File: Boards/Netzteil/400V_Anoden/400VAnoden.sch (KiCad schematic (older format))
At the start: 42 parts, among them P1 Drossel, P2 450V_AC, P3 CONN_4, P4 -120V_AC, P5 CONN_4, Q1 2SC2979

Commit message: Layouting...
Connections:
- wire segments 63 -> 61
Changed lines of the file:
@@
 EESchema Schematic File Version 2
+LIBS:400VAnoden-rescue
 LIBS:power
 LIBS:device
@@
 	8500 2700 8500 2600
 $Comp
-L GND #PWR10
+L GND-RESCUE-400VAnoden #PWR10
 U 1 1 55C60758
 P 8500 3250
@@
 $EndComp
 $Comp
-L GND #PWR8
+L GND-RESCUE-400VAnoden #PWR8
 U 1 1 55C607C2
 P 8100 2500
@@
 $EndComp
 $Comp
-L GND #PWR3
+L GND-RESCUE-400VAnoden #PWR3
 U 1 1 55C6080F
 P 1550 2250
@@
 $EndComp
 $Comp
-L GND #PWR4
+L GND-RESCUE-400VAnoden #PWR4
 U 1 1 55C60A98
 P 4350 2500
@@
 $EndComp
 $Comp
-L GND #PWR5
+L GND-RESCUE-400VAnoden #PWR5
 U 1 1 55C60AE5
 P 4950 2500
@@
 $EndComp
 $Comp
-L GND #PWR6
+L GND-RESCUE-400VAnoden #PWR6
 U 1 1 55C60B32
 P 6900 2500
@@
 $EndComp
 $Comp
-L GND #PWR7
+L GND-RESCUE-400VAnoden #PWR7
 U 1 1 55C60B7F
 P 7500 2500
@@
 $EndComp
 $Comp
-L GND #PWR1
+L GND-RESCUE-400VAnoden #PWR1
 U 1 1 55C60BCC
 P 5450 2000
@@
 $EndComp
 $Comp
-L GND #PWR2
+L GND-RESCUE-400VAnoden #PWR2
 U 1 1 55C60C19
 P 6250 2000
@@
 $EndComp
 Wire Wire Line
-	6000 1600 9050 1600
+	6000 1600 9400 1600
 Connection ~ 8100 1600
 Wire Wire Line
@@
 Wire Wire Line
 	8500 3250 8500 3100
-Wire Wire Line
-	9050 1600 9400 1600
 Wire Wire Line
 	9400 1600 9400 2500
@@
 Connection ~ 4250 4100
 $Comp
-L GND #PWR12
+L GND-RESCUE-400VAnoden #PWR12
 U 1 1 55C62E8C
 P 4250 4550
@@
 $EndComp
 $Comp
-L GND #PWR13
+L GND-RESCUE-400VAnoden #PWR13
 U 1 1 55C62EAA
 P 4850 4550
@@
 $EndComp
 Wire Wire Line
-	3800 4100 8950 4100
+	3800 4100 9400 4100
 Wire Wire Line
 	4250 4400 4250 4550
@@
 Connection ~ 4850 4100
 Wire Wire Line
-	8950 4100 9400 4100
-Wire Wire Line
 	9400 4100 9400 2800
 Wire Wire Line
 	9400 2800 9650 2800
 $Comp
-L GND #PWR9
+L GND-RESCUE-400VAnoden #PWR9
 U 1 1 55C6439E
 P 9600 3000
@@
 $EndComp
 $Comp
-L GND #PWR14
+L GND-RESCUE-400VAnoden #PWR14
 U 1 1 55C6CC4E
 P 1450 4750
@@
 Connection ~ 9600 3450
 $Comp
-L GND #PWR11
+L GND-RESCUE-400VAnoden #PWR11
 U 1 1 55D9E0ED
 P 9600 3750

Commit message: Work in Progress
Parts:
- removed P3, P5: CONN_4, MiniUniversalMate-N-LokSockets_13Aug2012:MiniUniversalMate-N-LokSocket_4PinVertical_13Aug2012, symbol CONN_4
- added P3, P5: CONN_3, Connectors_Mini-Universal:MiniUniversalMate-N-LokSocket_3PinVertical, symbol CONN_3
- D5: symbol ZENER -> ZENER-RESCUE-400VAnoden
- D6: symbol LED -> LED-RESCUE-400VAnoden
- P2: value 450V_AC -> 320V_AC
- P4: value -120V_AC -> 133V_AC
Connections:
- net labels added: +450V_DC, -180V_DC
- wire segments 61 -> 58

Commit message: Work in Progress
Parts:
- C1, C11, C12, C14, C15, C16, C2, C4, C5, C7, C8: symbol C -> Device:C
- C10, C13, C3, C6, C9: symbol CP -> Device:CP
- D1, D2, D3, D4: symbol D_Schottky -> Device:D_Schottky
- D10, D7, D8, D9: symbol D -> Device:D
- D5: symbol ZENER-RESCUE-400VAnoden -> 400VAnoden-rescue:ZENER-RESCUE-400VAnoden
- D6: symbol LED-RESCUE-400VAnoden -> 400VAnoden-rescue:LED-RESCUE-400VAnoden
- F1, F3: symbol F_Small -> 400VAnoden-rescue:F_Small
- P1, P2, P4: symbol CONN_2 -> borniers:CONN_2
- P3, P5: symbol CONN_3 -> borniers:CONN_3
- Q1: symbol Q_NPN_BCE -> Device:Q_NPN_BCE
- R1, R2, R3, R4, R5, R6, R7, R8: symbol R -> Device:R
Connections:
- wire segments 58 -> 92

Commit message: Converted to Kicad 5.1 and Layout changes
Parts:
- C1, C11, C12, C15, C16, C2, C7, C8: footprint Capacitor-Wima-FKP1-1600v:Capacitor-Wima-FKP1-1600v-R15B5 -> Capacitor_THT:C_Rect_L18.0mm_W5.0mm_P15.00mm_FKS3_FKP3
- C10, C6: footprint w_capacitors:CP_35x40mm -> Capacitor_THT:CP_Radial_D35.0mm_P10.00mm_SnapIn
- C13: footprint w_capacitors:CPA_16x31MM -> Capacitor_THT:CP_Radial_D16.0mm_P7.50mm
- C14, C4, C5: footprint Capacitor-Wima-MKP10-630v:Capacitor-Wima-MKP10-630v-R27K5B17 -> Capacitor_THT:C_Rect_L41.5mm_W20.0mm_P37.50mm_MKS4
- C3, C9: footprint w_capacitors:CP_22x25mm -> Capacitor_THT:CP_Radial_D22.0mm_P10.00mm_SnapIn
- D1, D2, D3, D4: footprint Diodes_ThroughHole:Diode_TO-220_Vertical -> Package_TO_SOT_THT:TO-220-2_Vertical
- D10, D7, D8, D9: footprint w_pth_diodes:diode_do41 -> Diode_THT:D_DO-41_SOD81_P10.16mm_Horizontal
- D5: footprint w_pth_diodes:diode_do35 -> Diode_THT:D_DO-35_SOD27_P10.16mm_Horizontal
- D6: footprint LEDs:LED-5MM -> LED_THT:LED_D5.0mm
- P1, P2, P4: footprint MiniUniversalMate-N-LokSockets_13Aug2012:MiniUniversalMate-N-LokSocket_2PinVertical_12Aug2012 -> Connector_TE-Connectivity:TE_MATE-N-LOK_1-770866-x_1x02_P4.14mm_Vertical; symbol borniers:CONN_2 -> 400VAnoden-rescue:CONN_2-borniers
- P3, P5: footprint Connectors_Mini-Universal:MiniUniversalMate-N-LokSocket_3PinVertical -> Connector_TE-Connectivity:TE_MATE-N-LOK_1-770870-x_1x03_P4.14mm_Vertical; symbol borniers:CONN_3 -> 400VAnoden-rescue:CONN_3-borniers
- Q1: footprint w_to:to220-horiz_5770 -> Package_TO_SOT_THT:TO-220-3_Horizontal_TabDown
- R1, R2, R3, R4, R5, R6, R7, R8: footprint Resistors_ThroughHole:Resistor_Horizontal_RM10mm -> Resistor_THT:R_Axial_DIN0207_L6.3mm_D2.5mm_P10.16mm_Horizontal

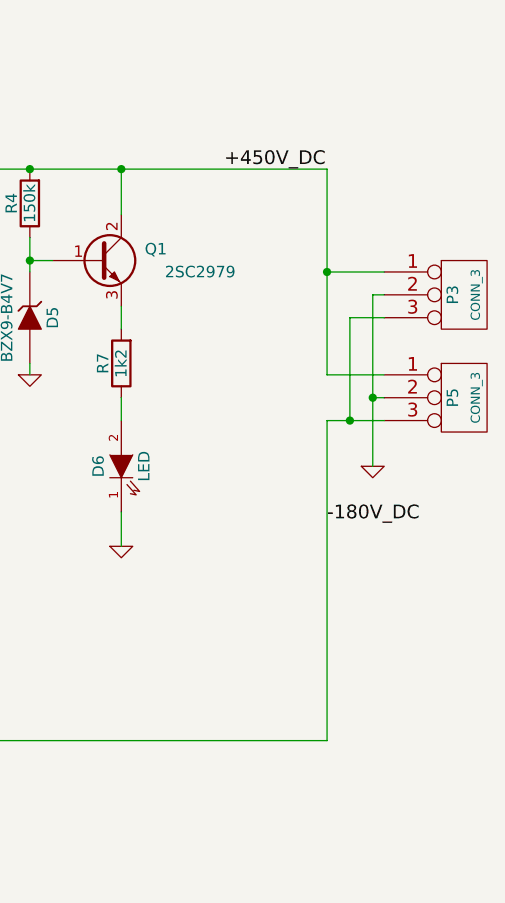
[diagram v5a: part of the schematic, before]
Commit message: Layout changes, Supply connector changes, Mounting holes
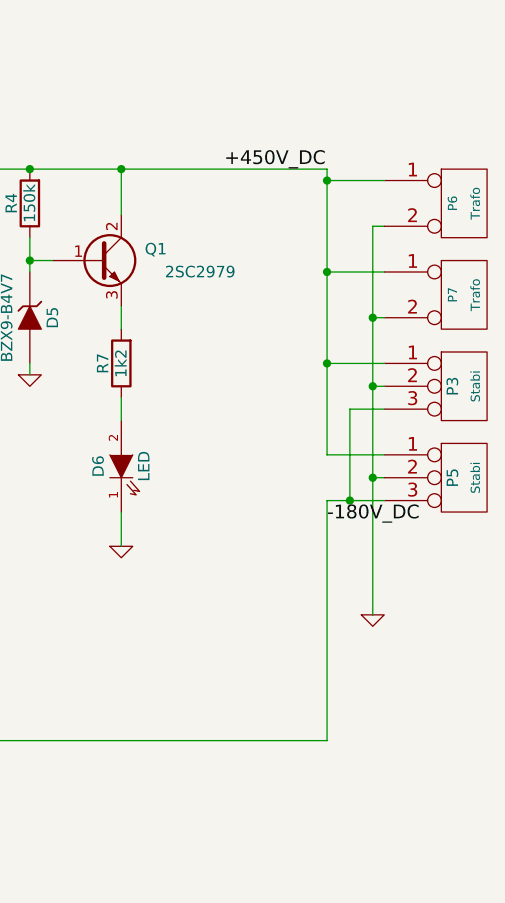
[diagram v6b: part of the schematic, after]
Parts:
- added P6, P7: Trafo, Connector_TE-Connectivity:TE_MATE-N-LOK_1-770866-x_1x02_P4.14mm_Vertical, symbol 400VAnoden-rescue:CONN_2-borniers
- P3, P5: value CONN_3 -> Stabi
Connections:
- net +450V_DC: now also P6.1 (P1), P7.1 (P1)
- net GND: now also P6.2 (P2), P7.2 (P2)
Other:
- moved on the sheet: P3, P5
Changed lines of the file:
@@
 L 400VAnoden-rescue:GND-RESCUE-400VAnoden #PWR012
 U 1 1 55C6439E
-P 9600 2900
-F 0 "#PWR012" H 9600 2900 30  0001 C CNN
-F 1 "GND" H 9600 2830 30  0001 C CNN
-F 2 "" H 9600 2900 60  0000 C CNN
-F 3 "" H 9600 2900 60  0000 C CNN
-	1    9600 2900
+P 9600 3550
+F 0 "#PWR012" H 9600 3550 30  0001 C CNN
+F 1 "GND" H 9600 3480 30  0001 C CNN
+F 2 "" H 9600 3550 60  0000 C CNN
+F 3 "" H 9600 3550 60  0000 C CNN
+	1    9600 3550
 	1    0    0    -1
 $EndComp
@@
 Connection ~ 4850 4100
 Wire Wire Line
-	9400 2700 9400 4100
+	9400 3050 9400 4100
 Wire Wire Line
 	4350 2400 4350 2500
@@
 	2550 4000 2550 4100
 Wire Wire Line
-	9400 2500 9650 2500
+	9400 2850 9650 2850
 $Comp
 L 400VAnoden-rescue:CONN_3-borniers P5
 U 1 1 5A14516E
-P 10000 2600
-F 0 "P5" V 9950 2600 50  0000 C CNN
-F 1 "CONN_3" V 10050 2600 40  0000 C CNN
-F 2 "Connector_TE-Connectivity:TE_MATE-N-LOK_1-770870-x_1x03_P4.14mm_Vertical" H 10000 2600 60  0001 C CNN
-F 3 "" H 10000 2600 60  0001 C CNN
-	1    10000 2600
-	1    0    0    -1
-$EndComp
-Wire Wire Line
-	9650 2600 9600 2600
-Wire Wire Line
-	9600 2150 9600 2600
-Wire Wire Line
-	9650 2700 9500 2700
-Wire Wire Line
-	9400 1600 9400 2050
+P 10000 2950
+F 0 "P5" V 9950 2950 50  0000 C CNN
+F 1 "Stabi" V 10050 2950 40  0000 C CNN
+F 2 "Connector_TE-Connectivity:TE_MATE-N-LOK_1-770870-x_1x03_P4.14mm_Vertical" H 10000 2950 60  0001 C CNN
+F 3 "" H 10000 2950 60  0001 C CNN
+	1    10000 2950
+	1    0    0    -1
+$EndComp
+Wire Wire Line
+	9650 2950 9600 2950
+Wire Wire Line
+	9600 2550 9600 2950
+Wire Wire Line
+	9650 3050 9500 3050
+Wire Wire Line
+	9400 1600 9400 1650
 $Comp
 L 400VAnoden-rescue:CONN_3-borniers P3
 U 1 1 5A14612F
+P 10000 2550
+F 0 "P3" V 9950 2550 50  0000 C CNN
+F 1 "Stabi" V 10050 2550 40  0000 C CNN
+F 2 "Connector_TE-Connectivity:TE_MATE-N-LOK_1-770870-x_1x03_P4.14mm_Vertical" H 10000 2550 60  0001 C CNN
+F 3 "" H 10000 2550 60  0001 C CNN
+	1    10000 2550
+	1    0    0    -1
+$EndComp
+Wire Wire Line
+	6000 1600 6250 1600
+Wire Wire Line
+	9650 2450 9400 2450
+Connection ~ 9400 2450
+Wire Wire Line
+	9650 2550 9600 2550
+Connection ~ 9600 2950
+Wire Wire Line
+	9650 2650 9500 2650
+Wire Wire Line
+	9500 2650 9500 3050
+Connection ~ 9500 3050
+Wire Wire Line
+	4350 1600 4950 1600
+Wire Wire Line
+	4950 1600 5450 1600
+Wire Wire Line
+	5450 1600 5800 1600
+Wire Wire Line
+	6250 1600 6900 1600
+Wire Wire Line
+	6900 1600 7500 1600
+Wire Wire Line
+	4950 2000 4950 2100
+Wire Wire Line
+	4350 2000 4350 2100
+Wire Wire Line
+	7500 1600 8100 1600
+Wire Wire Line
+	7500 2000 7500 2100
+Wire Wire Line
+	6900 2000 6900 2100
+Wire Wire Line
+	8100 2000 8100 2050
+Wire Wire Line
+	8100 1600 8500 1600
+Wire Wire Line
+	8500 1600 9400 1600
+Wire Wire Line
+	4250 4100 3800 4100
+Wire Wire Line
+	4850 4100 4250 4100
+Wire Wire Line
+	2650 1200 2950 1200
+Wire Wire Line
+	2150 1200 2650 1200
+Wire Wire Line
+	2650 2000 2950 2000
+Wire Wire Line
+	2150 2000 2650 2000
+Wire Wire Line
+	2650 1600 2650 1700
+Wire Wire Line
+	2150 1600 2150 1700
+Wire Wire Line
+	1850 2000 2150 2000
+Wire Wire Line
+	1850 1200 2150 1200
+Wire Wire Line
+	2550 3700 2850 3700
+Wire Wire Line
+	2050 3700 2550 3700
+Wire Wire Line
+	2550 4500 2850 4500
+Wire Wire Line
+	2050 4500 2550 4500
+Wire Wire Line
+	2550 4100 2550 4200
+Wire Wire Line
+	2050 4100 2050 4200
+Wire Wire Line
+	1750 4500 2050 4500
+Wire Wire Line
+	1750 3700 2050 3700
+Wire Wire Line
+	9400 2450 9400 2850
+Wire Wire Line
+	9600 2950 9600 3550
+Wire Wire Line
+	9500 3050 9400 3050
+$Comp
+L 400VAnoden-rescue:CONN_2-borniers P7
+U 1 1 5DA42FCE
 P 10000 2150
-F 0 "P3" V 9950 2150 50  0000 C CNN
-F 1 "CONN_3" V 10050 2150 40  0000 C CNN
-F 2 "Connector_TE-Connectivity:TE_MATE-N-LOK_1-770870-x_1x03_P4.14mm_Vertical" H 10000 2150 60  0001 C CNN
-F 3 "" H 10000 2150 60  0001 C CNN
+F 0 "P7" V 9950 2150 40  0000 C CNN
+F 1 "Trafo" V 10050 2150 40  0000 C CNN
+F 2 "Connector_TE-Connectivity:TE_MATE-N-LOK_1-770866-x_1x02_P4.14mm_Vertical" H 10000 2150 60  0001 C CNN
+F 3 "" H 10000 2150 60  0000 C CNN
 	1    10000 2150
 	1    0    0    -1
 $EndComp
-Wire Wire Line
-	6000 1600 6250 1600
+$Comp
+L 400VAnoden-rescue:CONN_2-borniers P6
+U 1 1 5DA5BD03
+P 10000 1750
+F 0 "P6" V 9950 1750 40  0000 C CNN
+F 1 "Trafo" V 10050 1750 40  0000 C CNN
+F 2 "Connector_TE-Connectivity:TE_MATE-N-LOK_1-770866-x_1x02_P4.14mm_Vertical" H 10000 1750 60  0001 C CNN
+F 3 "" H 10000 1750 60  0000 C CNN
+	1    10000 1750
+	1    0    0    -1
+$EndComp
 Wire Wire Line
 	9650 2050 9400 2050
 Connection ~ 9400 2050
 Wire Wire Line
-	9650 2150 9600 2150
-Connection ~ 9600 2600
-Wire Wire Line
-	9650 2250 9500 2250
-Wire Wire Line
-	9500 2250 9500 2700
-Connection ~ 9500 2700
-Wire Wire Line
-	4350 1600 4950 1600
-Wire Wire Line
-	4950 1600 5450 1600
-Wire Wire Line
-	5450 1600 5800 1600
-Wire Wire Line
-	6250 1600 6900 1600
-Wire Wire Line
-	6900 1600 7500 1600
-Wire Wire Line
-	4950 2000 4950 2100
-Wire Wire Line
-	4350 2000 4350 2100
-Wire Wire Line
-	7500 1600 8100 1600
-Wire Wire Line
-	7500 2000 7500 2100
-Wire Wire Line
-	6900 2000 6900 2100
-Wire Wire Line
-	8100 2000 8100 2050
-Wire Wire Line
-	8100 1600 8500 1600
-Wire Wire Line
-	8500 1600 9400 1600
-Wire Wire Line
-	4250 4100 3800 4100
-Wire Wire Line
-	4850 4100 4250 4100
-Wire Wire Line
-	2650 1200 2950 1200
-Wire Wire Line
-	2150 1200 2650 1200
-Wire Wire Line
-	2650 2000 2950 2000
-Wire Wire Line
-	2150 2000 2650 2000
-Wire Wire Line
-	2650 1600 2650 1700
-Wire Wire Line
-	2150 1600 2150 1700
-Wire Wire Line
-	1850 2000 2150 2000
-Wire Wire Line
-	1850 1200 2150 1200
-Wire Wire Line
-	2550 3700 2850 3700
-Wire Wire Line
-	2050 3700 2550 3700
-Wire Wire Line
-	2550 4500 2850 4500
-Wire Wire Line
-	2050 4500 2550 4500
-Wire Wire Line
-	2550 4100 2550 4200
-Wire Wire Line
-	2050 4100 2050 4200
-Wire Wire Line
-	1750 4500 2050 4500
-Wire Wire Line
-	1750 3700 2050 3700
-Wire Wire Line
-	9400 2050 9400 2500
-Wire Wire Line
-	9600 2600 9600 2900
-Wire Wire Line
-	9500 2700 9400 2700
+	9400 2050 9400 2450
+Wire Wire Line
+	9650 1650 9400 1650
+Connection ~ 9400 1650
+Wire Wire Line
+	9400 1650 9400 2050
+Wire Wire Line
+	9600 2550 9600 2250
+Wire Wire Line
+	9600 2250 9650 2250
+Connection ~ 9600 2550
+Wire Wire Line
+	9600 2250 9600 1850
+Wire Wire Line
+	9600 1850 9650 1850
+Connection ~ 9600 2250
 $EndSCHEMATC

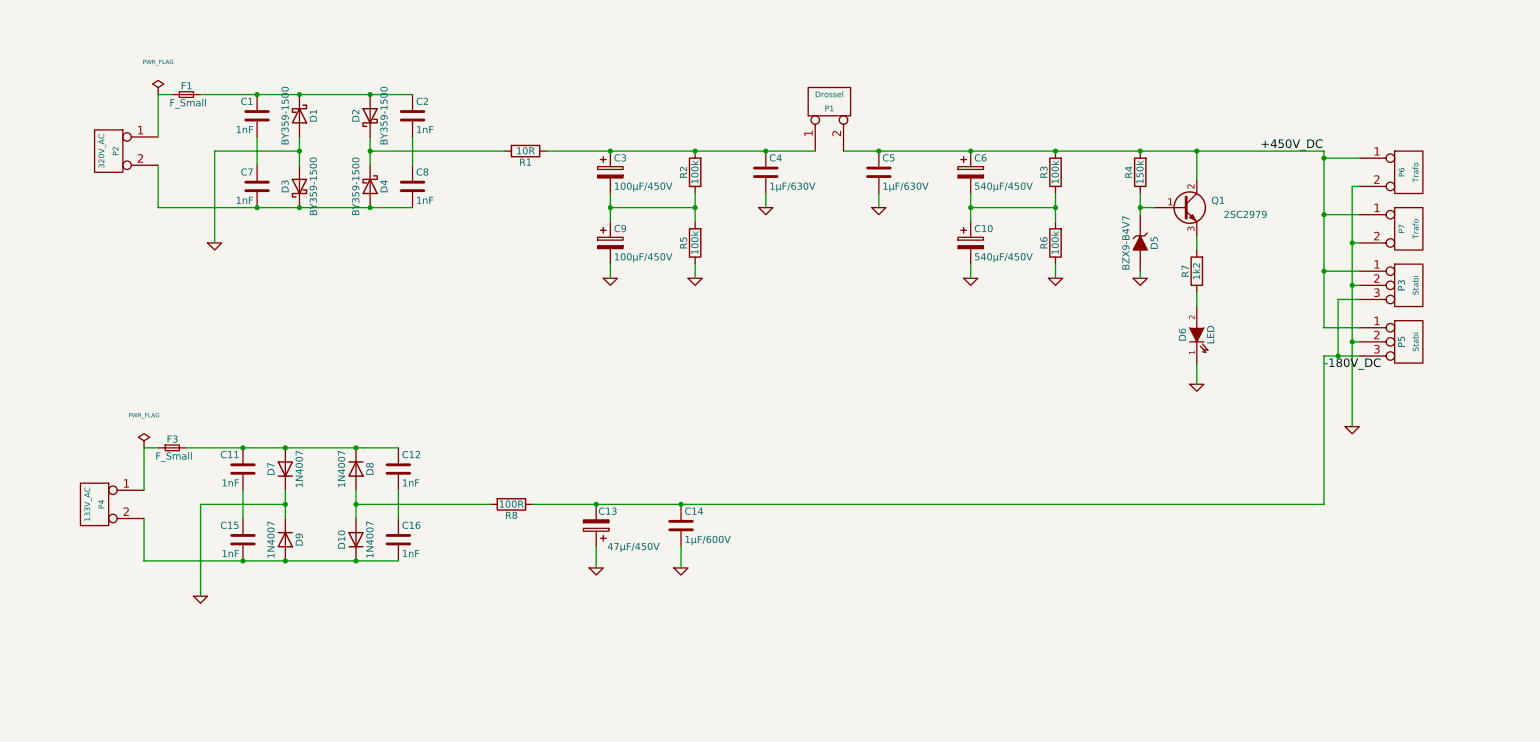
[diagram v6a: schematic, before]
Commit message: HV Switch on delay added
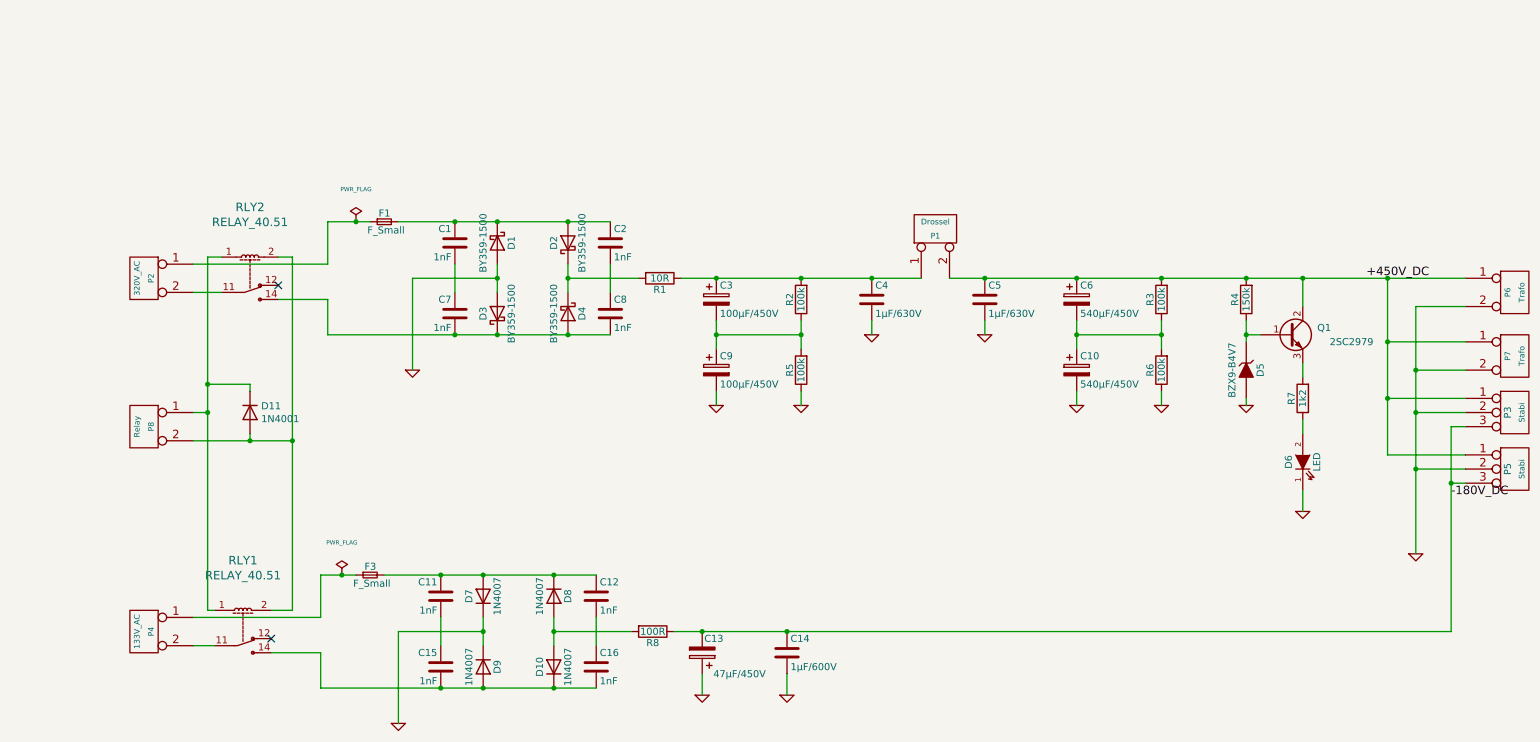
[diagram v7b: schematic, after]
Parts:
- added D11: 1N4001, Diode_THT:D_DO-41_SOD81_P10.16mm_Horizontal, symbol Device:D
- added P8: Relay, Connector_Molex:Molex_KK-254_AE-6410-02A_1x02_P2.54mm_Vertical, symbol 400VAnoden-rescue:CONN_2-borniers
- added RLY1, RLY2: RELAY_40.51, w_relay:relay_40.51, symbol w_relay:RELAY_40.51
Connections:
- net at C7.2, C8.2, D3.1 (K)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: now also RLY2.14; no longer P2.2 (P2)
- net at C15.2, C16.2, D10.1 (K)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: now also RLY1.14; no longer P4.2 (P2)
- new net: P2.2 (P2), RLY2.11
- new net: P4.2 (P2), RLY1.11
- new net: D11.1 (K), P8.1 (P1), RLY1.1, RLY2.1
- new net: D11.2 (A), P8.2 (P2), RLY1.2, RLY2.2
- no-connect marks 0 -> 2
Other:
- moved on the sheet: C1, C10, C11, C12, C13, C14, C15, C16, C2, C3, C4, C5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
